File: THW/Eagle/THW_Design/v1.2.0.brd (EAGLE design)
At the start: 100 x 200 mm, 24 parts

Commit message: More work
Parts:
- R_CURRENT: value (none) -> 100
- moved PAD1 3.00 mm to (17.0, 161.0)
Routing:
- added copper zone on layer 16, net GND
- removed copper zone on layer 16, net BSHEILD

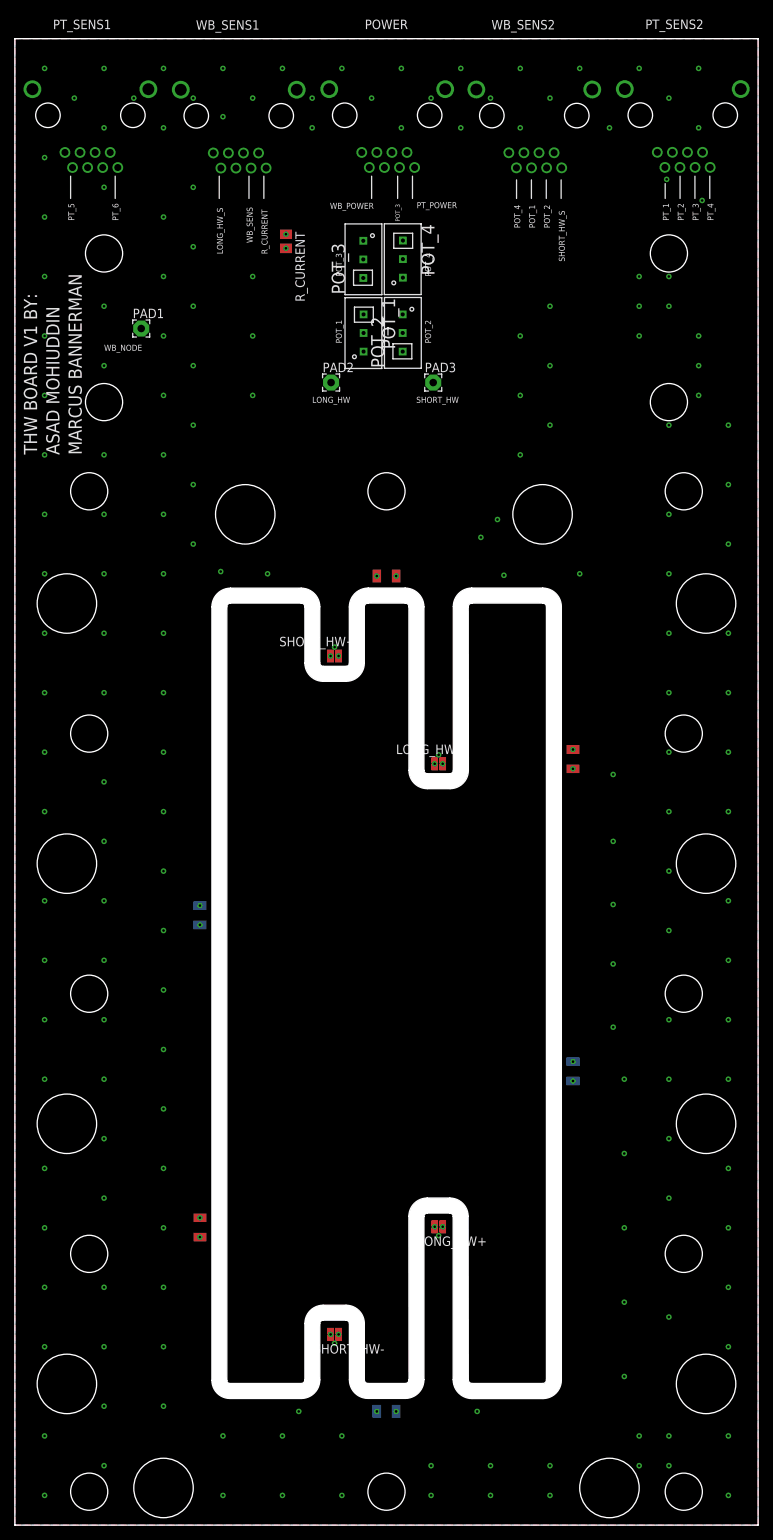
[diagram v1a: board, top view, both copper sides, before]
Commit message: fix sheild pin
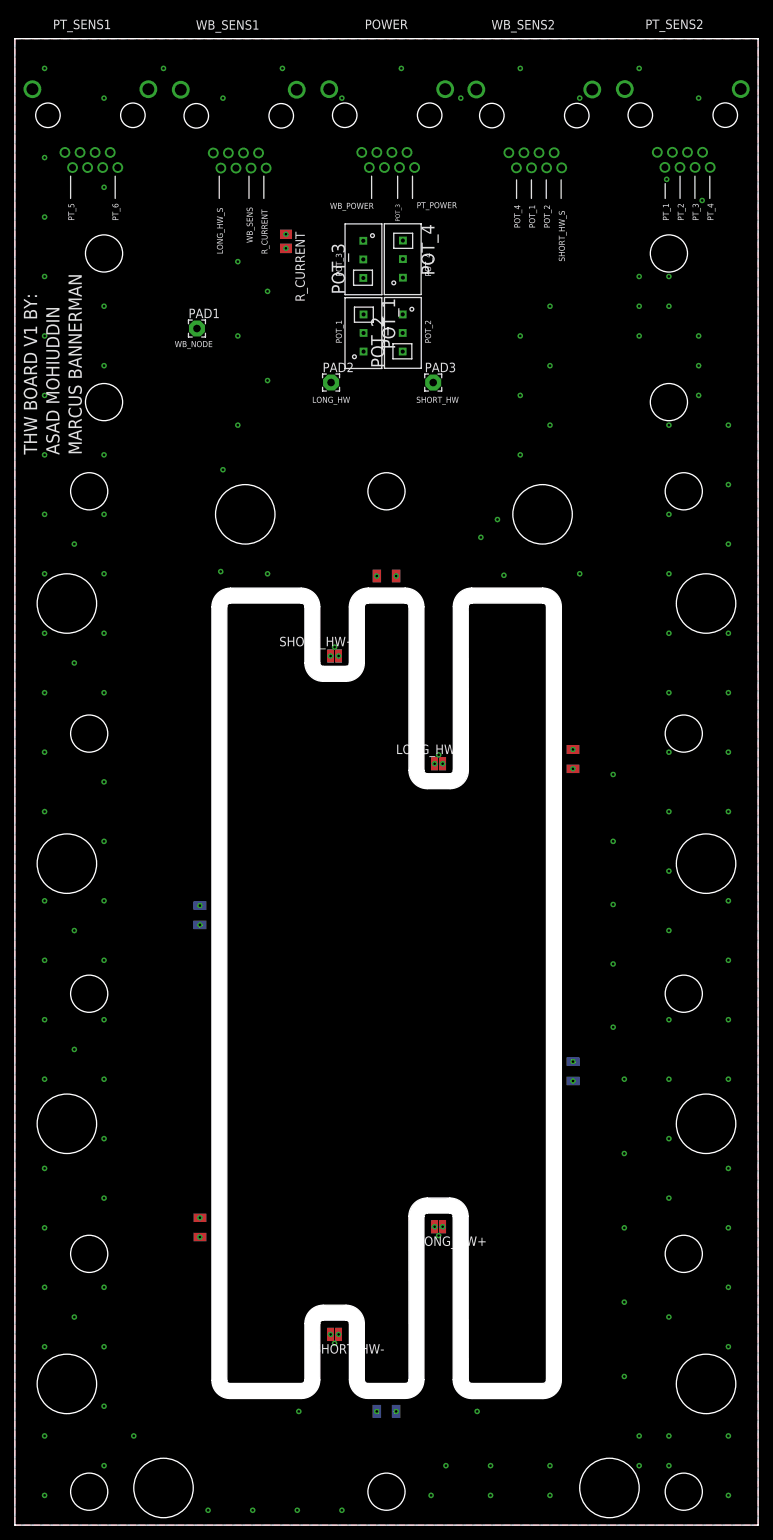
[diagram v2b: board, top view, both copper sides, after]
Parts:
- added LONG_HW+1, LONG_HW-1, SHORT_HW+1, SHORT_HW-1: WIREPOINT_1A, WIREPOINT:WIREPOINT
- moved PAD1 7.50 mm to (24.5, 161.0)
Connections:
- net N$1: now also LONG_HW-1.P$1, LONG_HW-1.P$2
- net N$7: now also SHORT_HW+1.P$1, SHORT_HW+1.P$2
- net SHORT_HW-: now also LONG_HW+1.P$1, LONG_HW+1.P$2, SHORT_HW-1.P$1, SHORT_HW-1.P$2
